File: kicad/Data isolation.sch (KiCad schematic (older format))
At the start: 102 parts, among them U601 SI8660, U602 SI8660, U603 SI8660, U604 SI8660, U605 SI8660, U606 SI8660

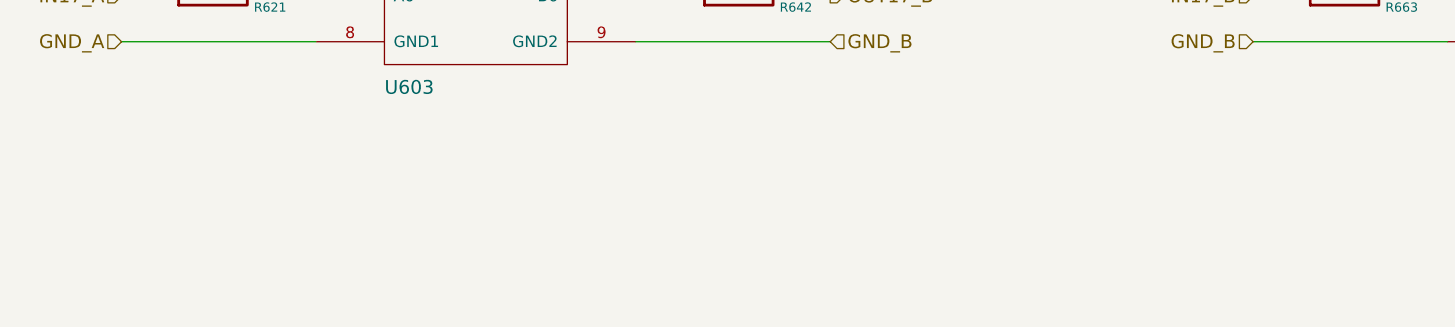
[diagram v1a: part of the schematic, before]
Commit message: Added note about A and B postfix to Data isolation sheet
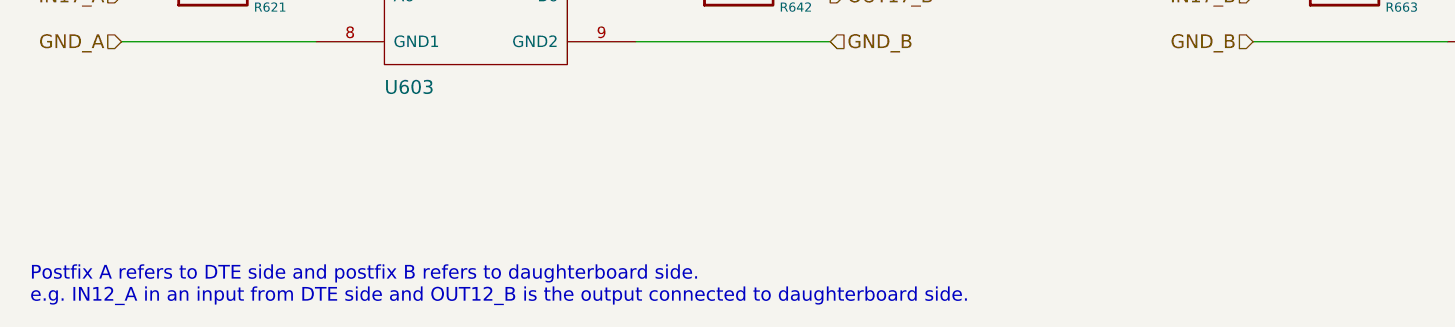
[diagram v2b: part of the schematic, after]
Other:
- note added: "Postfix A refers to DTE side and postfix B refers to daughterboard side.\ne.g. IN12_A in an input from DTE side and OUT12_B is the output connected to daughterboard side.\n"
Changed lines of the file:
@@
 	-1   0    0    -1
 $EndComp
+Text Notes 1400 7450 0    60   ~ 0
+Postfix A refers to DTE side and postfix B refers to daughterboard side.\ne.g. IN12_A in an input from DTE side and OUT12_B is the output connected to daughterboard side.\n
 $EndSCHEMATC
